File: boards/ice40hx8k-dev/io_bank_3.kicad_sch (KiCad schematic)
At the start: 22 parts, among them U1 ICE40HX8K-CT256

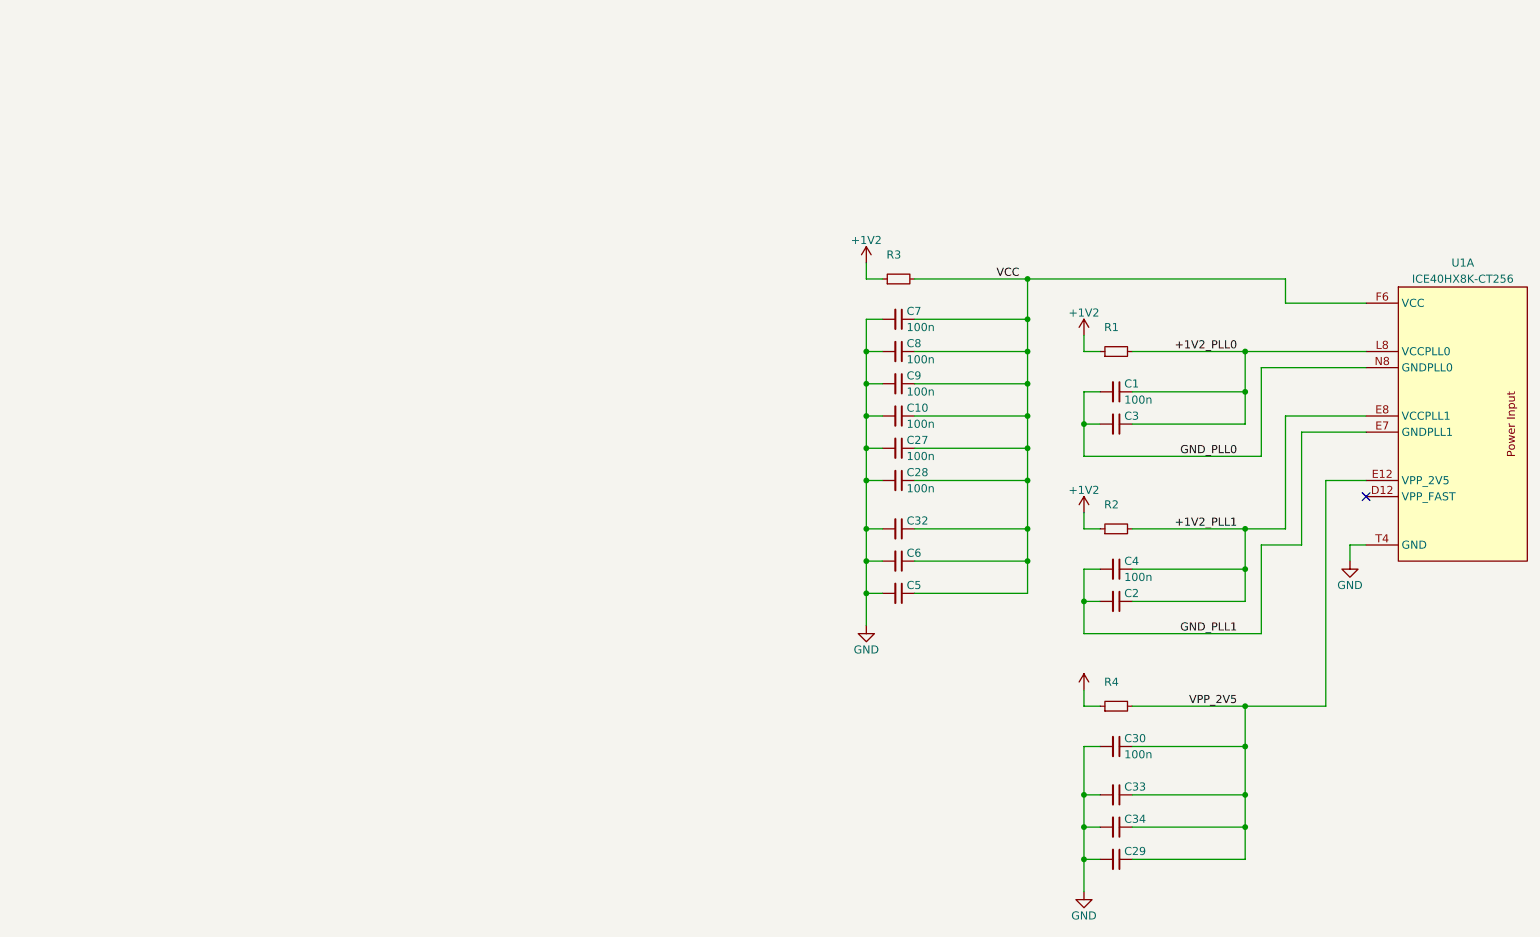
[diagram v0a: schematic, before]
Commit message: Split up schematic and label all nets.
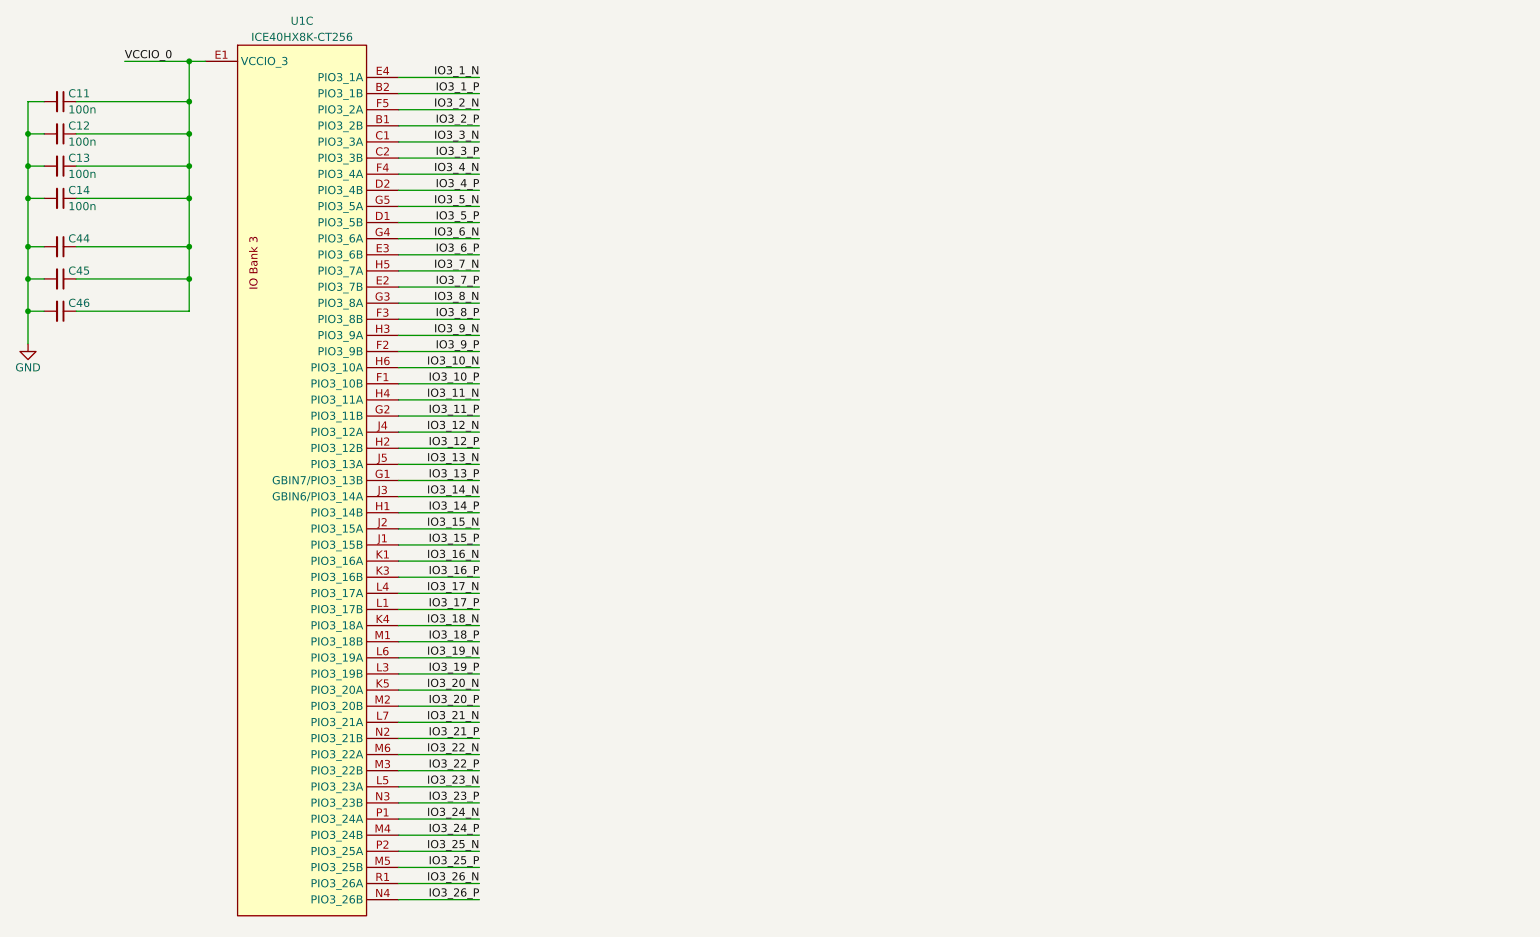
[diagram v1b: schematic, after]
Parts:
- removed C1, C10, C27, C28, C30, C4, C7, C8, C9: 100n, 0Local:C_SMD_0402_Pad0.5mm, symbol Device:C_Small
- removed C2, C29, C3, C32, C33, C34, C5, C6: (no value), 0Local:C_SMD_0402_Pad0.5mm, symbol Device:C_Small
- removed R1, R3: (no value), 0Local:R_SMD_0402_Pad0.5mm, symbol Device:R_Small
- removed R2, R4: (no value), symbol Device:R_Small
- removed U1: ICE40HX8K-CT256, 0Local:Lattice_caBGA-256_14x14mm_Layout16x16_P0.8mm_Ball0.4mm_Pad0.5mm_SMD, symbol 0Local:ICE40HX8K-CT256
- added C11, C12, C13, C14: 100n, 0Local:C_SMD_0402_Pad0.5mm, symbol Device:C_Small
- added C44, C45, C46: (no value), 0Local:C_SMD_0402_Pad0.5mm, symbol Device:C_Small
- added U1: ICE40HX8K-CT256, 0Local:Lattice_caBGA-256_14x14mm_Layout16x16_P0.8mm_Ball0.4mm_Pad0.5mm_SMD, symbol 0Local:ICE40HX8K-CT256
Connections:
- net GND: now also C11.2, C12.2, C13.2, C14.2, C44.2, C45.2, C46.2
- new net IO3_10_N: U1.H6 (PIO3_10A)
- new net IO3_10_P: U1.F1 (PIO3_10B)
- new net IO3_11_N: U1.H4 (PIO3_11A)
- new net IO3_11_P: U1.G2 (PIO3_11B)
- new net IO3_12_N: U1.J4 (PIO3_12A)
- new net IO3_12_P: U1.H2 (PIO3_12B)
- new net IO3_13_N: U1.J5 (PIO3_13A)
- new net IO3_13_P: U1.G1 (GBIN7/PIO3_13B)
- new net IO3_14_N: U1.J3 (GBIN6/PIO3_14A)
- new net IO3_14_P: U1.H1 (PIO3_14B)
- new net IO3_15_N: U1.J2 (PIO3_15A)
- new net IO3_15_P: U1.J1 (PIO3_15B)
- new net IO3_16_N: U1.K1 (PIO3_16A)
- new net IO3_16_P: U1.K3 (PIO3_16B)
- new net IO3_17_N: U1.L4 (PIO3_17A)
- new net IO3_17_P: U1.L1 (PIO3_17B)
- new net IO3_18_N: U1.K4 (PIO3_18A)
- new net IO3_18_P: U1.M1 (PIO3_18B)
- new net IO3_19_N: U1.L6 (PIO3_19A)
- new net IO3_19_P: U1.L3 (PIO3_19B)
- new net IO3_1_N: U1.E4 (PIO3_1A)
- new net IO3_1_P: U1.B2 (PIO3_1B)
- new net IO3_20_N: U1.K5 (PIO3_20A)
- new net IO3_20_P: U1.M2 (PIO3_20B)
- new net IO3_21_N: U1.L7 (PIO3_21A)
- new net IO3_21_P: U1.N2 (PIO3_21B)
- new net IO3_22_N: U1.M6 (PIO3_22A)
- new net IO3_22_P: U1.M3 (PIO3_22B)
- new net IO3_23_N: U1.L5 (PIO3_23A)
- new net IO3_23_P: U1.N3 (PIO3_23B)
- new net IO3_24_N: U1.P1 (PIO3_24A)
- new net IO3_24_P: U1.M4 (PIO3_24B)
- new net IO3_25_N: U1.P2 (PIO3_25A)
- new net IO3_25_P: U1.M5 (PIO3_25B)
- new net IO3_26_N: U1.R1 (PIO3_26A)
- new net IO3_26_P: U1.N4 (PIO3_26B)
- new net IO3_2_N: U1.F5 (PIO3_2A)
- new net IO3_2_P: U1.B1 (PIO3_2B)
- new net IO3_3_N: U1.C1 (PIO3_3A)
- new net IO3_3_P: U1.C2 (PIO3_3B)
- new net IO3_4_N: U1.F4 (PIO3_4A)
- new net IO3_4_P: U1.D2 (PIO3_4B)
- new net IO3_5_N: U1.G5 (PIO3_5A)
- new net IO3_5_P: U1.D1 (PIO3_5B)
- new net IO3_6_N: U1.G4 (PIO3_6A)
- new net IO3_6_P: U1.E3 (PIO3_6B)
- new net IO3_7_N: U1.H5 (PIO3_7A)
- new net IO3_7_P: U1.E2 (PIO3_7B)
- new net IO3_8_N: U1.G3 (PIO3_8A)
- new net IO3_8_P: U1.F3 (PIO3_8B)
- new net IO3_9_N: U1.H3 (PIO3_9A)
- new net IO3_9_P: U1.F2 (PIO3_9B)
- new net VCCIO_0: C11.1, C12.1, C13.1, C14.1, C44.1, C45.1, C46.1, U1.E1 (VCCIO_3), U1.G6 (VCCIO_3), U1.J6 (VCCIO_3), U1.N1 (VCCIO_3)
- no-connect marks 1 -> 0

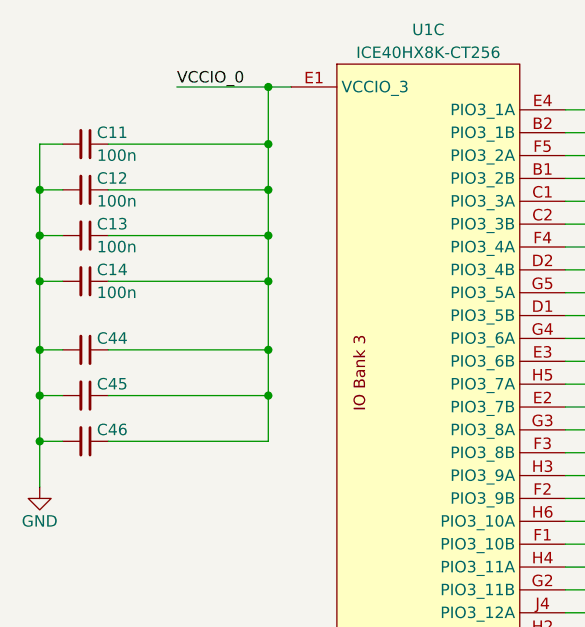
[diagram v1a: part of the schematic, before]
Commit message: Switch to 6 layers, add power fills under BGA.
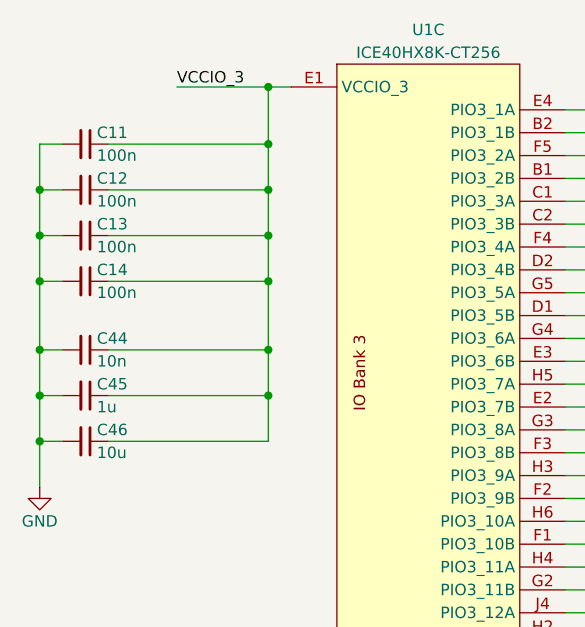
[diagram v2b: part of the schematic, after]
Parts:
- C44: value (none) -> 10n
- C45: value (none) -> 1u
- C46: value (none) -> 10u
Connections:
- net VCCIO_0 renamed VCCIO_3
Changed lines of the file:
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@@
     (effects (font (size 1.27 1.27)) (justify right bottom))
   )
-  (label "VCCIO_0" (at 33.02 27.94 0)
+  (label "VCCIO_3" (at 33.02 27.94 0)
     (effects (font (size 1.27 1.27)) (justify left bottom))
   )
@@
       (effects (font (size 1.27 1.27)) (justify left))
     )
-    (property "Value" "" (id 1) (at 24.13 58.42 90)
+    (property "Value" "10n" (id 1) (at 24.13 58.42 90)
       (effects (font (size 1.27 1.27)) (justify left))
     )
@@
       (effects (font (size 1.27 1.27)) (justify left))
     )
-    (property "Value" "" (id 1) (at 24.13 63.5 90)
+    (property "Value" "1u" (id 1) (at 24.13 63.5 90)
       (effects (font (size 1.27 1.27)) (justify left))
     )
@@
       (effects (font (size 1.27 1.27)) (justify left))
     )
-    (property "Value" "" (id 1) (at 24.13 68.58 90)
+    (property "Value" "10u" (id 1) (at 24.13 68.58 90)
       (effects (font (size 1.27 1.27)) (justify left))
     )

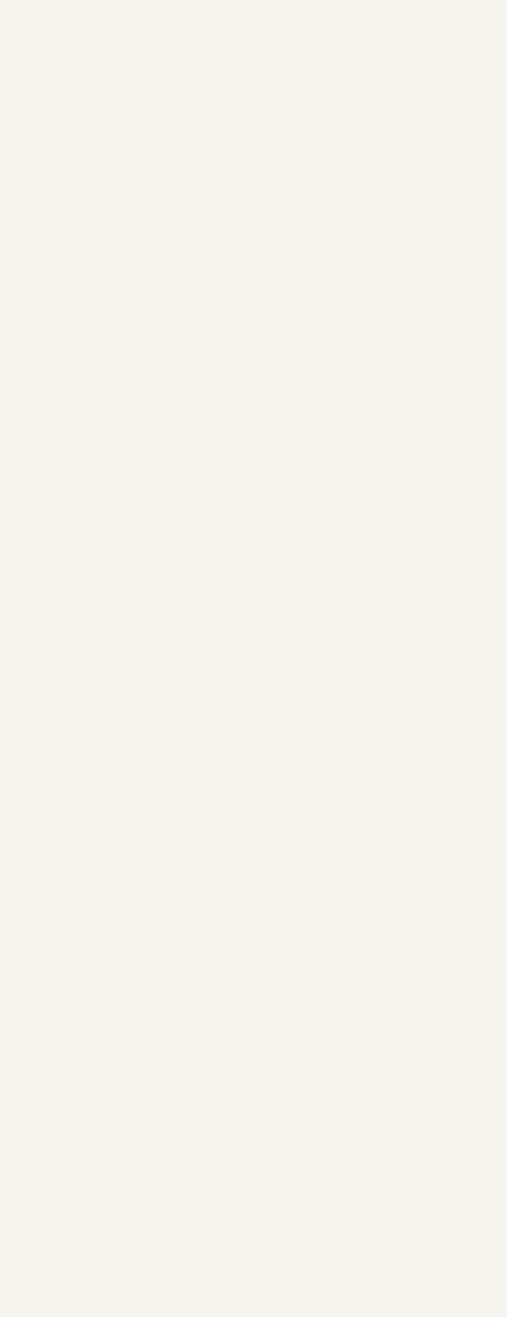
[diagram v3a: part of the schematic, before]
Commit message: Add Hirose connectors and standoffs.
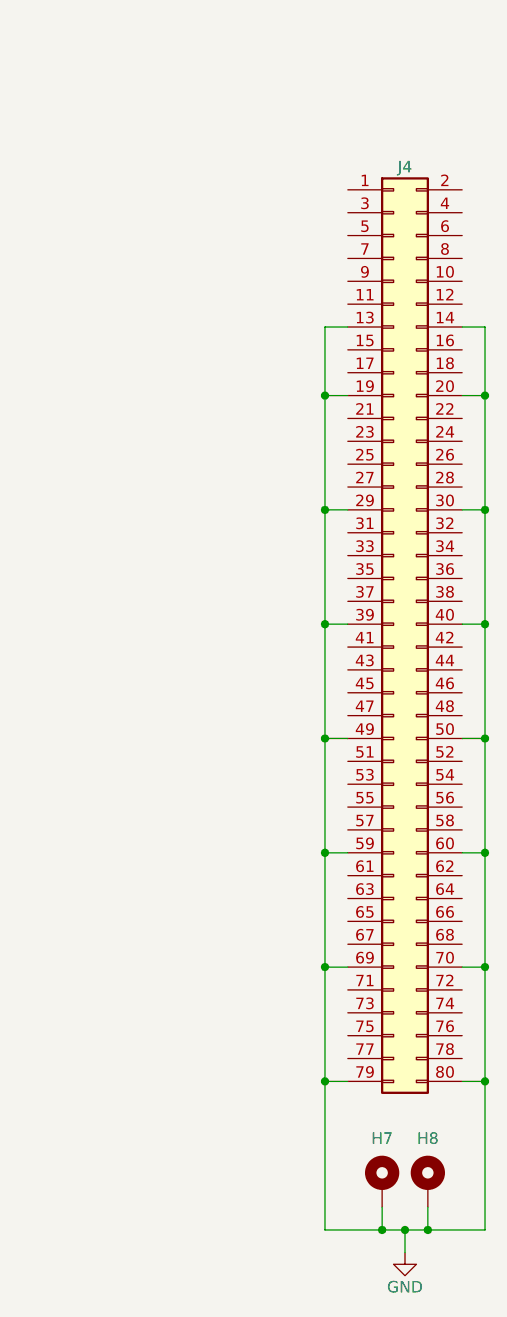
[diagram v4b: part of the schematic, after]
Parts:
- added H7, H8: 9774020633, Mounting_Wuerth:Mounting_Wuerth_WA-SMSI-M1.6_H2mm_9774020633, symbol Mechanical:MountingHole_Pad
- added J4: DF40HC(4.0)-80DS, 0Local:Hirose_DF40C-80DS, symbol Connector_Generic:Conn_02x40_Odd_Even
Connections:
- net GND: now also H7.1, H8.1, J4.13 (Pin_13), J4.14 (Pin_14), J4.19 (Pin_19), J4.20 (Pin_20), J4.29 (Pin_29), J4.30 (Pin_30), J4.39 (Pin_39), J4.40 (Pin_40), J4.49 (Pin_49), J4.50 (Pin_50), J4.59 (Pin_59), J4.60 (Pin_60), J4.69 (Pin_69), J4.70 (Pin_70), J4.79 (Pin_79), J4.80 (Pin_80)

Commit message: Switch to 4mm Hirose connectors and different mounting holes.
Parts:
- H7, H8: footprint Mounting_Wuerth:Mounting_Wuerth_WA-SMSI-M1.6_H2mm_9774020633 -> 0Local:MountingHole_2.2mm_M2_Pad6mm
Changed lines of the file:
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@@
       (effects (font (size 1.27 1.27)) hide)
     )
-    (property "Footprint" "Mounting_Wuerth:Mounting_Wuerth_WA-SMSI-M1.6_H2mm_9774020633" (id 2) (at 243.84 149.86 0)
+    (property "Footprint" "0Local:MountingHole_2.2mm_M2_Pad6mm" (id 2) (at 243.84 149.86 0)
       (effects (font (size 1.27 1.27)) hide)
     )
@@
       (effects (font (size 1.27 1.27)) hide)
     )
-    (property "Footprint" "Mounting_Wuerth:Mounting_Wuerth_WA-SMSI-M1.6_H2mm_9774020633" (id 2) (at 238.76 149.86 0)
+    (property "Footprint" "0Local:MountingHole_2.2mm_M2_Pad6mm" (id 2) (at 238.76 149.86 0)
       (effects (font (size 1.27 1.27)) hide)
     )
